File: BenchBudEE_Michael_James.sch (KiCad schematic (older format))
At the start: 0 parts

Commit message: Module 2.Unit 15
Defining you inputs and outputs
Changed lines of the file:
@@
 $EndDescr
 $Sheet
-S 850  6100 2000 1250
+S 1400 3100 2600 4400
 U 52F43D4E
 F0 "Arduino" 50
 F1 "Arduino.sch" 50
+F2 "Relay +" O R 4000 6500 60
+F3 "Relay -" I R 4000 6700 60
+F4 "MOSI" O R 4000 5100 60
+F5 "MISO" I R 4000 5350 60
+F6 "SCLK" O R 4000 5600 60
+F7 "CS_N" O R 4000 5900 60
+F8 "LED_EN" O R 4000 3850 60
+F9 "LED_FREQ" O R 4000 4100 60
+F10 "FAN_EN" O R 4000 3200 60
+F11 "TACH_MEAS" I R 4000 3350 60
 $EndSheet
 $Sheet
@@
 F2 "TC IN +" I R 9700 4400 60
 F3 "TC IN -" I R 9700 4600 60
+F4 "MOSI" I L 8000 4350 60
+F5 "MISO" O L 8000 4550 60
+F6 "SCLK" I L 8000 4750 60
+F7 "CS_N" I L 8000 4950 60
 $EndSheet
 $Sheet
@@
 F0 "Relay" 50
 F1 "Relay.sch" 50
+F2 "DIN +" I L 8050 6050 60
+F3 "DN -" O L 8050 6350 60
+F4 "Relay +" I R 9750 6000 60
+F5 "Relay -" O R 9750 6300 60
 $EndSheet
 $Sheet
-S 900  1000 1650 1200
+S 1500 950  2650 1450
 U 52F43DCC
 F0 "Power" 50
@@
 F0 "LED Driver" 50
 F1 "LED Driver.sch" 50
+F2 "EN" I L 8000 2800 60
+F3 "FREQ" I L 8000 3150 60
+F4 "String +" O R 9600 2800 60
+F5 "String -" I R 9600 3100 60
 $EndSheet
 $Sheet
@@
 F0 "Fan" 50
 F1 "Fan.sch" 50
+F2 "Power+" I R 9600 1300 60
+F3 "Power-" I R 9600 1550 60
+F4 "Tach" I R 9600 1800 60
+F5 "Tach_out" O L 8000 1300 60
+F6 "Fan_In" I L 8000 1650 60
 $EndSheet
 $Sheet

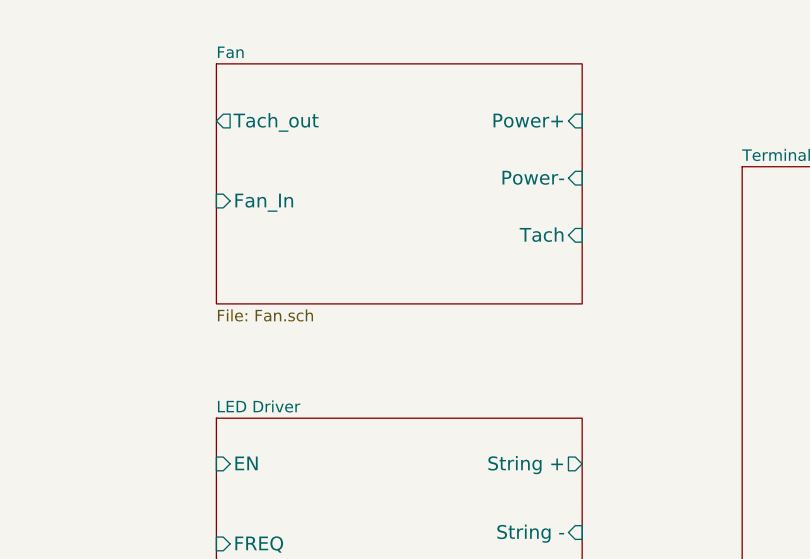
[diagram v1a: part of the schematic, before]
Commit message: Module 3. Unit 4
Create the rough out of the Fan module
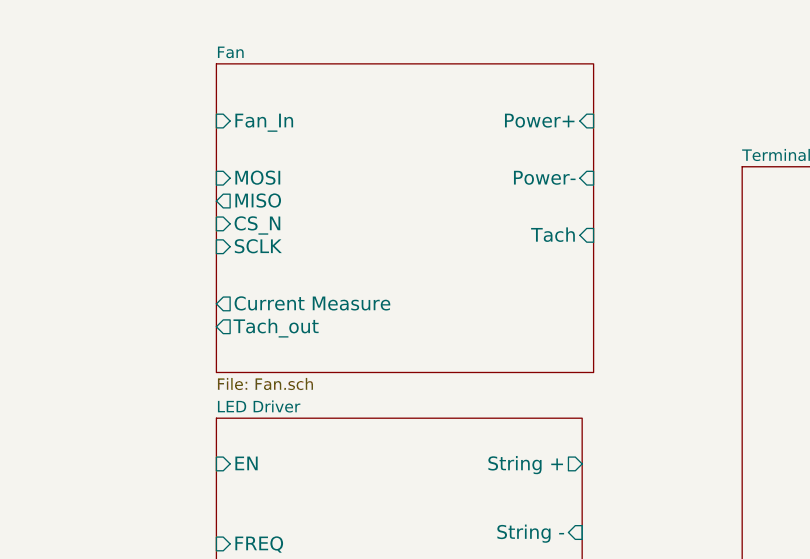
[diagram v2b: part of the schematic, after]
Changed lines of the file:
@@
 Sheet 1 8
 Title ""
-Date "7 feb 2014"
+Date "10 feb 2014"
 Rev ""
 Comp ""
@@
 $EndSheet
 $Sheet
-S 8000 1050 1600 1050
+S 8000 1050 1650 1350
 U 52F43E12
 F0 "Fan" 50
 F1 "Fan.sch" 50
-F2 "Power+" I R 9600 1300 60
-F3 "Power-" I R 9600 1550 60
-F4 "Tach" I R 9600 1800 60
-F5 "Tach_out" O L 8000 1300 60
-F6 "Fan_In" I L 8000 1650 60
+F2 "Power+" I R 9650 1300 60
+F3 "Power-" I R 9650 1550 60
+F4 "Tach" I R 9650 1800 60
+F5 "Tach_out" O L 8000 2200 60
+F6 "Fan_In" I L 8000 1300 60
+F7 "Current Measure" O L 8000 2100 60
+F8 "MOSI" I L 8000 1550 60
+F9 "MISO" O L 8000 1650 60
+F10 "CS_N" I L 8000 1750 60
+F11 "SCLK" I L 8000 1850 60
 $EndSheet
 $Sheet

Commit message: M3 U5
Power protection and filtering
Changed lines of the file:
@@
 $Descr A4 11693 8268
 encoding utf-8
-Sheet 1 8
+Sheet 1 9
 Title ""
-Date "10 feb 2014"
+Date "12 feb 2014"
 Rev ""
 Comp ""
@@
 $EndSheet
 $Sheet
-S 1500 950  2650 1450
+S 900  800  1100 1500
 U 52F43DCC
 F0 "Power" 50
@@
 F1 "TerminalBlock.sch" 50
 $EndSheet
+$Sheet
+S 3550 750  1200 1500
+U 52FAF1BC
+F0 "PowerAdjustmentMonitor" 50
+F1 "PowerAdjustmentMonitor.sch" 50
+$EndSheet
 $EndSCHEMATC

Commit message: M3 U7
LED Driver
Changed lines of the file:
@@
 F0 "LED Driver" 50
 F1 "LED Driver.sch" 50
-F2 "EN" I L 8000 2800 60
-F3 "FREQ" I L 8000 3150 60
-F4 "String +" O R 9600 2800 60
-F5 "String -" I R 9600 3100 60
+F2 "String +" O R 9600 2800 60
+F3 "String -" I R 9600 3100 60
+F4 "LED_EN_PWM" I L 8000 2900 60
 $EndSheet
 $Sheet

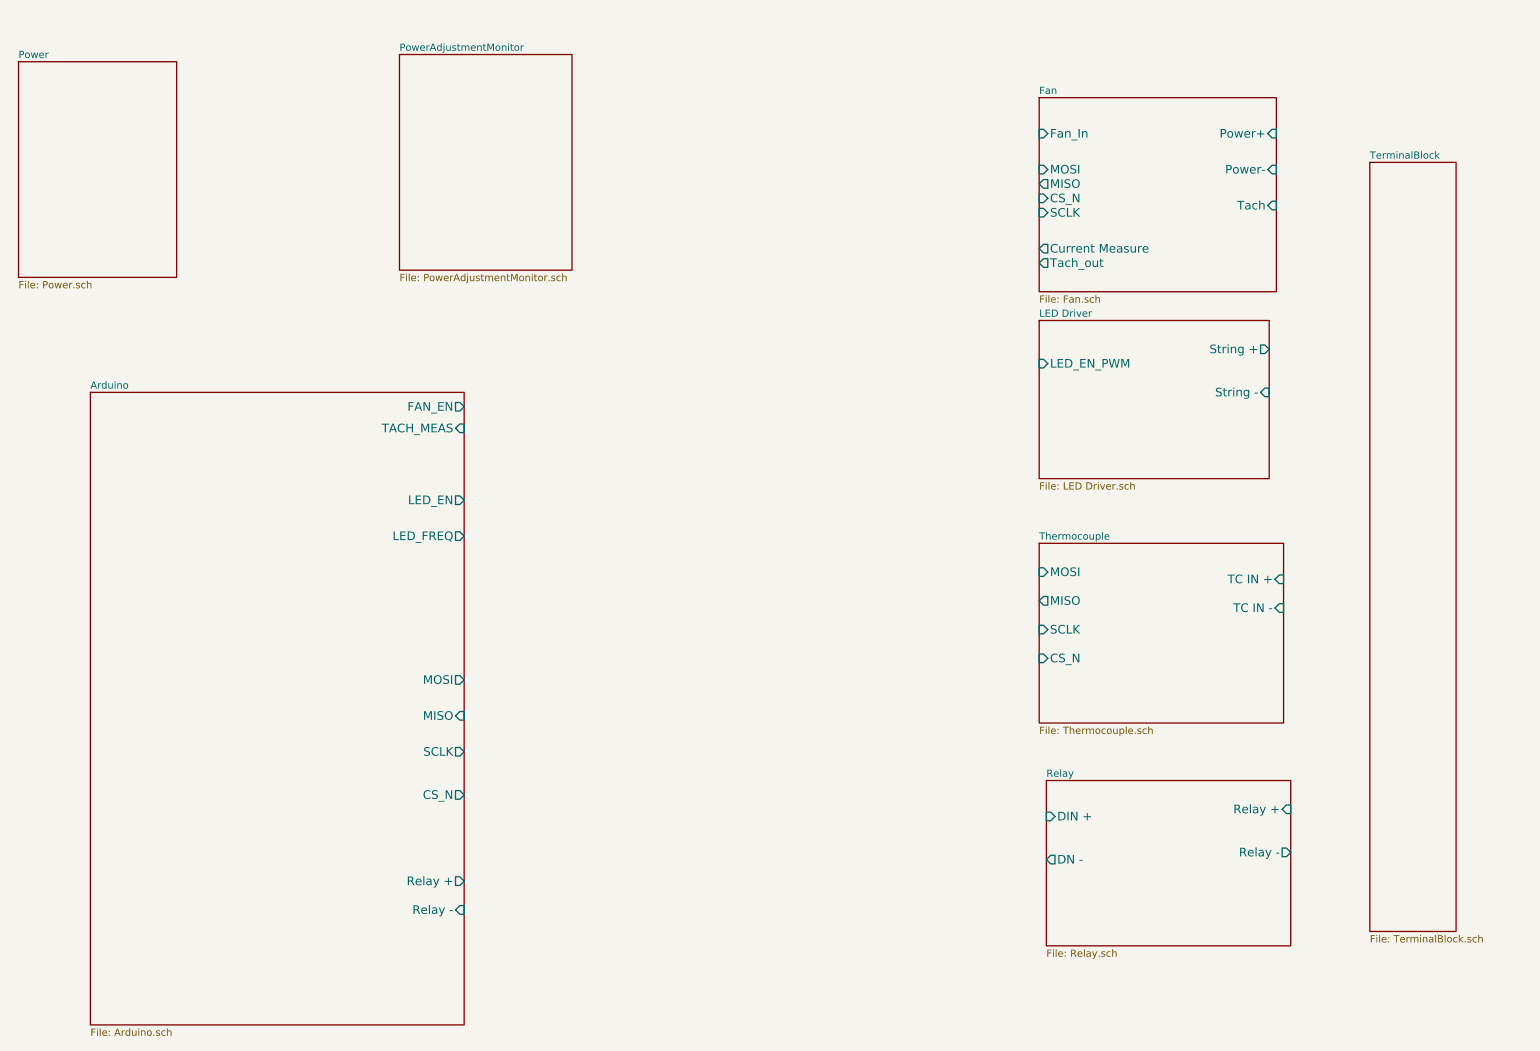
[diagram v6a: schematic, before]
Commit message: M3 U8
Arduino Module.   My Arduino Pin numbering does not matches Chris'.  I
believe he missed one in the video
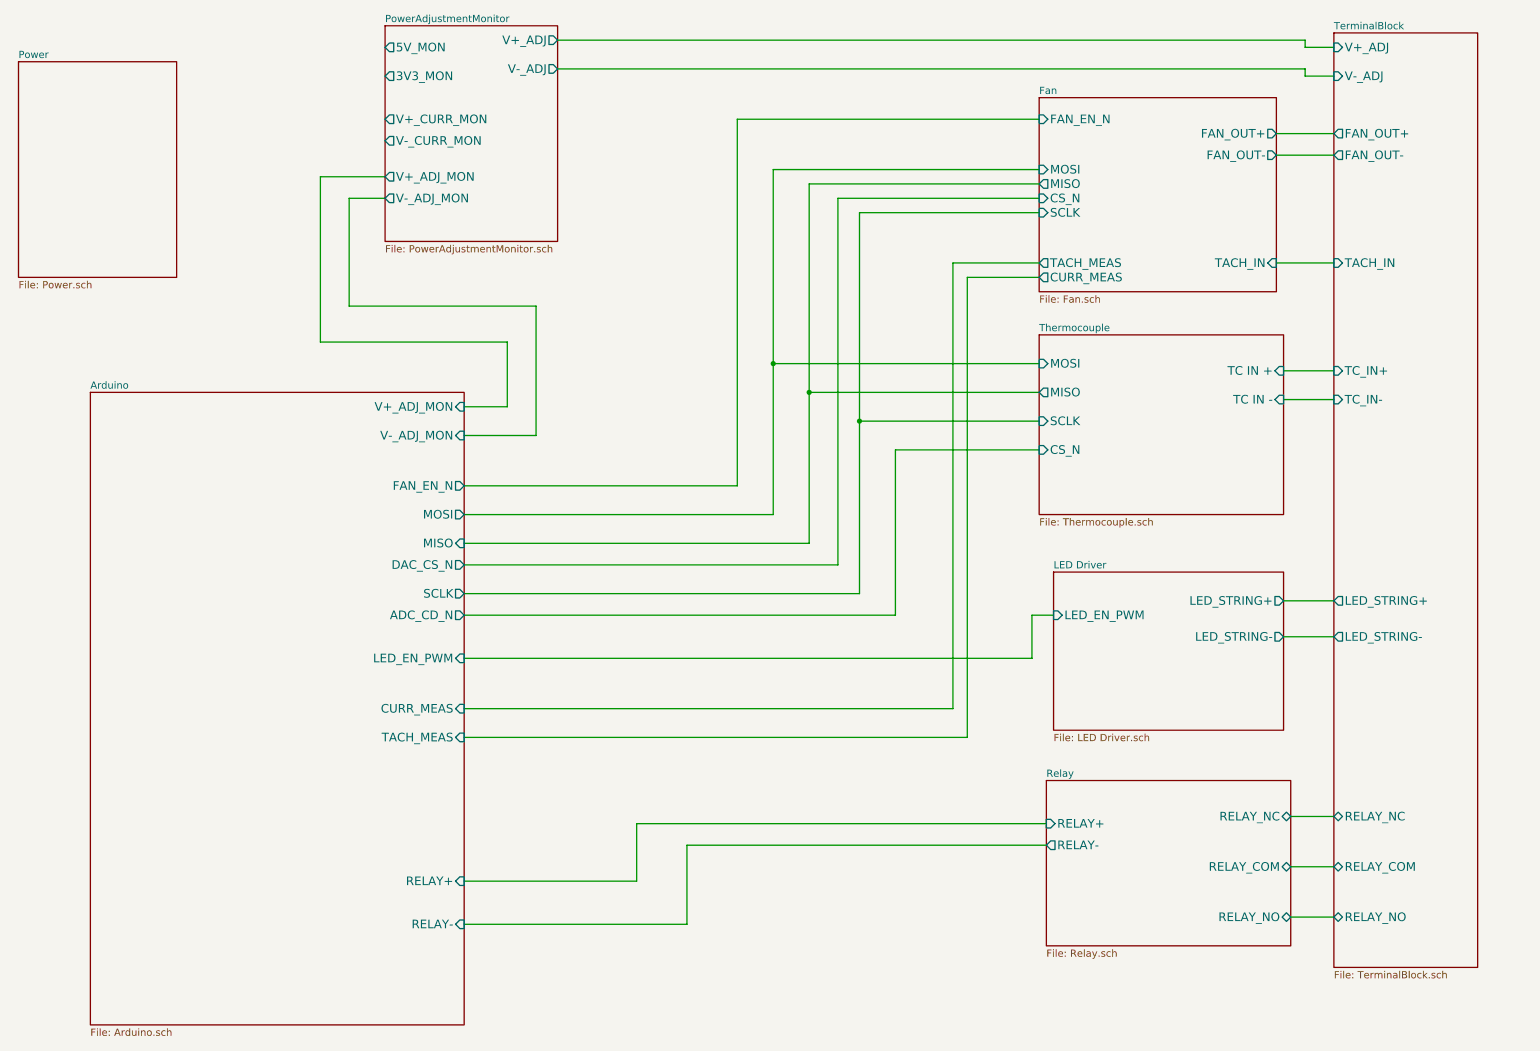
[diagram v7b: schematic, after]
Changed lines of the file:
@@
 Sheet 1 9
 Title ""
-Date "14 feb 2014"
+Date "15 feb 2014"
 Rev ""
 Comp ""
@@
 F0 "Arduino" 50
 F1 "Arduino.sch" 50
-F2 "Relay +" O R 4000 6500 60
-F3 "Relay -" I R 4000 6700 60
-F4 "MOSI" O R 4000 5100 60
-F5 "MISO" I R 4000 5350 60
-F6 "SCLK" O R 4000 5600 60
-F7 "CS_N" O R 4000 5900 60
-F8 "LED_EN" O R 4000 3850 60
-F9 "LED_FREQ" O R 4000 4100 60
-F10 "FAN_EN" O R 4000 3200 60
-F11 "TACH_MEAS" I R 4000 3350 60
-$EndSheet
-$Sheet
-S 8000 4150 1700 1250
+F2 "MOSI" O R 4000 3950 60
+F3 "MISO" I R 4000 4150 60
+F4 "SCLK" O R 4000 4500 60
+F5 "TACH_MEAS" I R 4000 5500 60
+F6 "RELAY+" I R 4000 6500 60
+F7 "RELAY-" I R 4000 6800 60
+F8 "FAN_EN_N" O R 4000 3750 60
+F9 "CURR_MEAS" I R 4000 5300 60
+F10 "V+_ADJ_MON" I R 4000 3200 60
+F11 "V-_ADJ_MON" I R 4000 3400 60
+F12 "LED_EN_PWM" I R 4000 4950 60
+F13 "DAC_CS_N" O R 4000 4300 60
+F14 "ADC_CD_N" O R 4000 4650 60
+$EndSheet
+$Sheet
+S 8000 2700 1700 1250
 U 52F43DA8
 F0 "Thermocouple" 50
 F1 "Thermocouple.sch" 50
-F2 "TC IN +" I R 9700 4400 60
-F3 "TC IN -" I R 9700 4600 60
-F4 "MOSI" I L 8000 4350 60
-F5 "MISO" O L 8000 4550 60
-F6 "SCLK" I L 8000 4750 60
-F7 "CS_N" I L 8000 4950 60
+F2 "TC IN +" I R 9700 2950 60
+F3 "TC IN -" I R 9700 3150 60
+F4 "MOSI" I L 8000 2900 60
+F5 "MISO" O L 8000 3100 60
+F6 "SCLK" I L 8000 3300 60
+F7 "CS_N" I L 8000 3500 60
 $EndSheet
 $Sheet
@@
 F0 "Relay" 50
 F1 "Relay.sch" 50
-F2 "DIN +" I L 8050 6050 60
-F3 "DN -" O L 8050 6350 60
-F4 "Relay +" I R 9750 6000 60
-F5 "Relay -" O R 9750 6300 60
+F2 "RELAY_NC" B R 9750 6050 60
+F3 "RELAY_NO" B R 9750 6750 60
+F4 "RELAY_COM" B R 9750 6400 60
+F5 "RELAY+" I L 8050 6100 60
+F6 "RELAY-" O L 8050 6250 60
 $EndSheet
 $Sheet
@@
 $EndSheet
 $Sheet
-S 8000 2600 1600 1100
+S 8100 4350 1600 1100
 U 52F43DF4
 F0 "LED Driver" 50
 F1 "LED Driver.sch" 50
-F2 "String +" O R 9600 2800 60
-F3 "String -" I R 9600 3100 60
-F4 "LED_EN_PWM" I L 8000 2900 60
+F2 "LED_EN_PWM" I L 8100 4650 60
+F3 "LED_STRING+" O R 9700 4550 60
+F4 "LED_STRING-" O R 9700 4800 60
 $EndSheet
 $Sheet
@@
 F0 "Fan" 50
 F1 "Fan.sch" 50
-F2 "Power+" I R 9650 1300 60
-F3 "Power-" I R 9650 1550 60
-F4 "Tach" I R 9650 1800 60
-F5 "Tach_out" O L 8000 2200 60
-F6 "Fan_In" I L 8000 1300 60
-F7 "Current Measure" O L 8000 2100 60
-F8 "MOSI" I L 8000 1550 60
-F9 "MISO" O L 8000 1650 60
-F10 "CS_N" I L 8000 1750 60
-F11 "SCLK" I L 8000 1850 60
-$EndSheet
-$Sheet
-S 10300 1500 600  5350
+F2 "MOSI" I L 8000 1550 60
+F3 "MISO" O L 8000 1650 60
+F4 "CS_N" I L 8000 1750 60
+F5 "SCLK" I L 8000 1850 60
+F6 "FAN_OUT+" O R 9650 1300 60
+F7 "FAN_OUT-" O R 9650 1450 60
+F8 "TACH_IN" I R 9650 2200 60
+F9 "TACH_MEAS" O L 8000 2200 60
+F10 "FAN_EN_N" I L 8000 1200 60
+F11 "CURR_MEAS" O L 8000 2300 60
+$EndSheet
+$Sheet
+S 3450 550  1200 1500
+U 52FAF1BC
+F0 "PowerAdjustmentMonitor" 50
+F1 "PowerAdjustmentMonitor.sch" 50
+F2 "V+_ADJ" O R 4650 650 60
+F3 "V-_ADJ" O R 4650 850 60
+F4 "3V3_MON" O L 3450 900 60
+F5 "5V_MON" O L 3450 700 60
+F6 "V+_ADJ_MON" O L 3450 1600 60
+F7 "V-_ADJ_MON" O L 3450 1750 60
+F8 "V+_CURR_MON" O L 3450 1200 60
+F9 "V-_CURR_MON" O L 3450 1350 60
+$EndSheet
+$Sheet
+S 10050 600  1000 6500
 U 52F43E3C
 F0 "TerminalBlock" 50
 F1 "TerminalBlock.sch" 50
-$EndSheet
-$Sheet
-S 3550 750  1200 1500
-U 52FAF1BC
-F0 "PowerAdjustmentMonitor" 50
-F1 "PowerAdjustmentMonitor.sch" 50
-$EndSheet
+F2 "V+_ADJ" I L 10050 700 60
+F3 "V-_ADJ" I L 10050 900 60
+F4 "FAN_OUT+" O L 10050 1300 60
+F5 "FAN_OUT-" O L 10050 1450 60
+F6 "TACH_IN" I L 10050 2200 60
+F7 "LED_STRING+" O L 10050 4550 60
+F8 "LED_STRING-" O L 10050 4800 60
+F9 "TC_IN+" I L 10050 2950 60
+F10 "TC_IN-" I L 10050 3150 60
+F11 "RELAY_COM" B L 10050 6400 60
+F12 "RELAY_NC" B L 10050 6050 60
+F13 "RELAY_NO" B L 10050 6750 60
+$EndSheet
+Wire Wire Line
+	4650 650  9850 650
+Wire Wire Line
+	9850 650  9850 700
+Wire Wire Line
+	9850 700  10050 700
+Wire Wire Line
+	4650 850  9850 850
+Wire Wire Line
+	9850 850  9850 900
+Wire Wire Line
+	9850 900  10050 900
+Wire Wire Line
+	9650 1300 10050 1300
+Wire Wire Line
+	9650 1450 10050 1450
+Wire Wire Line
+	10050 6050 9750 6050
+Wire Wire Line
+	9750 6400 10050 6400
+Wire Wire Line
+	10050 6750 9750 6750
+Wire Wire Line
+	10050 2200 9650 2200
+Wire Wire Line
+	4000 3200 4300 3200
+Wire Wire Line
+	4300 3200 4300 2750
+Wire Wire Line
+	4300 2750 3000 2750
+Wire Wire Line
+	3000 2750 3000 1600
+Wire Wire Line
+	3000 1600 3450 1600
+Wire Wire Line
+	4000 3400 4500 3400
+Wire Wire Line
+	4500 3400 4500 2500
+Wire Wire Line
+	4500 2500 3200 2500
+Wire Wire Line
+	3200 2500 3200 1750
+Wire Wire Line
+	3200 1750 3450 1750
+Wire Wire Line
+	4000 3750 5900 3750
+Wire Wire Line
+	5900 3750 5900 1200
+Wire Wire Line
+	5900 1200 8000 1200
+Wire Wire Line
+	4000 3950 6150 3950
+Wire Wire Line
+	6150 3950 6150 1550
+Wire Wire Line
+	6150 1550 8000 1550
+Wire Wire Line
+	6400 4150 4000 4150
+Wire Wire Line
+	6400 1650 6400 4150
+Wire Wire Line
+	6400 1650 8000 1650
+Wire Wire Line
+	6600 4300 6600 1750
+Wire Wire Line
+	6600 1750 8000 1750
+Wire Wire Line
+	8000 1850 6750 1850
+Wire Wire Line
+	6750 1850 6750 4500
+Wire Wire Line
+	6750 4500 4000 4500
+Wire Wire Line
+	9700 2950 10050 2950
+Wire Wire Line
+	10050 3150 9700 3150
+Wire Wire Line
+	8000 2900 6150 2900
+Connection ~ 6150 2900
+Wire Wire Line
+	8000 3100 6400 3100
+Connection ~ 6400 3100
+Wire Wire Line
+	6600 4300 4000 4300
+Wire Wire Line
+	4000 4650 7000 4650
+Wire Wire Line
+	7000 4650 7000 3500
+Wire Wire Line
+	7000 3500 8000 3500
+Wire Wire Line
+	8000 3300 6750 3300
+Connection ~ 6750 3300
+Wire Wire Line
+	8050 6100 5200 6100
+Wire Wire Line
+	5200 6100 5200 6500
+Wire Wire Line
+	5200 6500 4000 6500
+Wire Wire Line
+	4000 6800 5550 6800
+Wire Wire Line
+	5550 6800 5550 6250
+Wire Wire Line
+	5550 6250 8050 6250
+Wire Wire Line
+	10050 4550 9700 4550
+Wire Wire Line
+	9700 4800 10050 4800
+Wire Wire Line
+	4000 5300 7400 5300
+Wire Wire Line
+	7400 5300 7400 2200
+Wire Wire Line
+	7400 2200 8000 2200
+Wire Wire Line
+	8100 4650 7950 4650
+Wire Wire Line
+	7950 4650 7950 4950
+Wire Wire Line
+	7950 4950 4000 4950
+Wire Wire Line
+	8000 2300 7500 2300
+Wire Wire Line
+	7500 2300 7500 5500
+Wire Wire Line
+	7500 5500 4000 5500
 $EndSCHEMATC
